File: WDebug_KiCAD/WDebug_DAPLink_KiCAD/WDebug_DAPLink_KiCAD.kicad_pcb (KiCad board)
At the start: 2 copper layers, 55 x 34 mm, 42 parts, among them J1 Conn_01x04, J2 Conn_02x04_UART_SW, J3 Conn_01x20_Female, J4 Conn_01x05_Male, J5 01x18_Female_Fan, P1 USB_C_Plug_USB2.0, SW1 SW_Rst, U1 AZ1117-3.3, U2 STM32F103C8Tx, Y1 8MHz

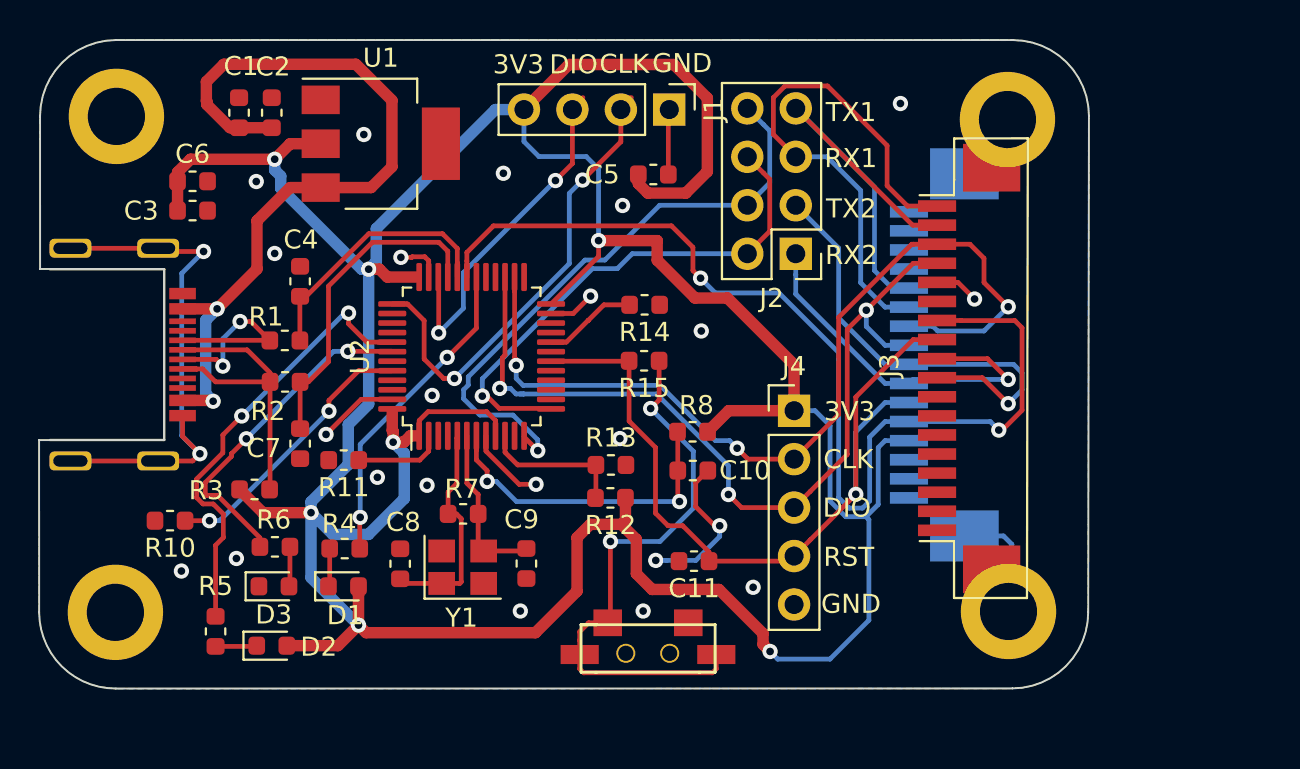
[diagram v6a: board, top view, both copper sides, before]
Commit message: WDebug_KiCAD_V1.3 修改串口RX和TX相反，16pin接口定义相反
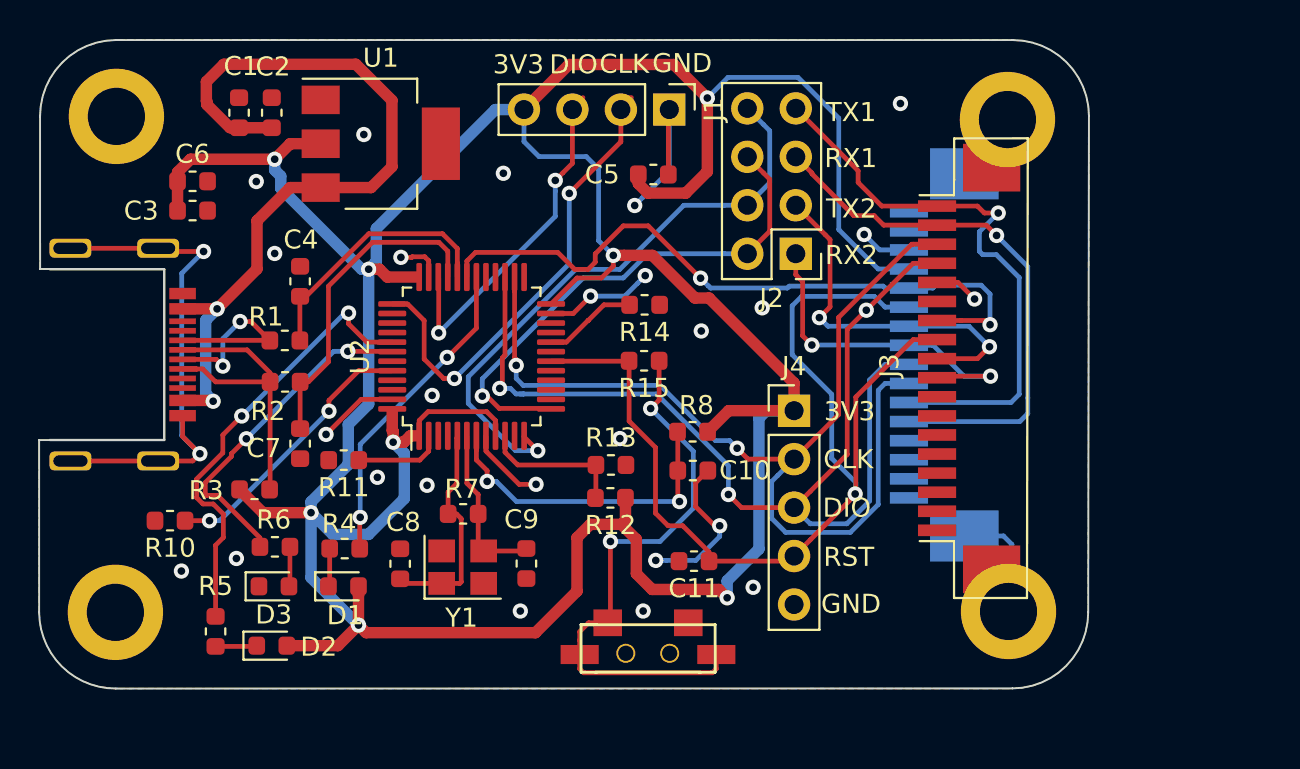
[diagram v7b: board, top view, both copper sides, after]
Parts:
- J5: footprint WDebug_KiCAD:1x16_P1.0mm -> WDebug_DAPLink:1x16_P1.0mm
- P1: footprint WDebug_KiCAD:USB-Type-C -> WDebug_DAPLink:USB-Type-C
- SW1: footprint WDebug_KiCAD:SWITCH_PUSH -> WDebug_DAPLink:SWITCH_PUSH
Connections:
- J3 pad 10: /RX2 -> /TX2
- J3 pad 17: /TX1 -> /RX1
- J3 pad 18: /RX1 -> /TX1
- J3 pad 9: /TX2 -> /RX2
- J5 pad 10: /RX2 -> /TX2
- J5 pad 5: /TX1 -> /RX1
- J5 pad 6: /RX1 -> /TX1
- J5 pad 9: /TX2 -> /RX2
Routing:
- net /T_SWO: track 55.7 -> 36.2 mm
- net /TG_RST: track 43.2 -> 55.3 mm
- net GND: track 36.9 -> 48.7 mm, vias 23 -> 26
- net /T_SWDIO: track 45.2 -> 55.3 mm
- net /TX1: track 22.3 -> 30.4 mm, vias 0 -> 1
- net /T_SWCLK: track 48.5 -> 54.7 mm, vias 3 -> 2
- net /TX2: track 23.9 -> 19.4 mm, vias 1 -> 2
- net /RX2: track 19.5 -> 18.0 mm, vias 1 -> 2
- net /T_TX: track 32.1 -> 31.5 mm
- net /RX1: track 28.3 -> 28.7 mm, vias 0 -> 1
- net +3V3: track 195.5 -> 195.8 mm, vias 7 -> 8
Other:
- board text added: "WDebug_DAPLink_V1.3 Chenweipeng 20200417"
- board text removed: "WDebug_DAPLink_V1.2 Chenweipeng 20200413"

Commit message: WDebug_DAPLink V1.4 1 修改 16Pin接口SWCLK和SWDIO反了。 2 3.3V不直接连接到16pin和18pin接口 3 AMS1117换成线性3819
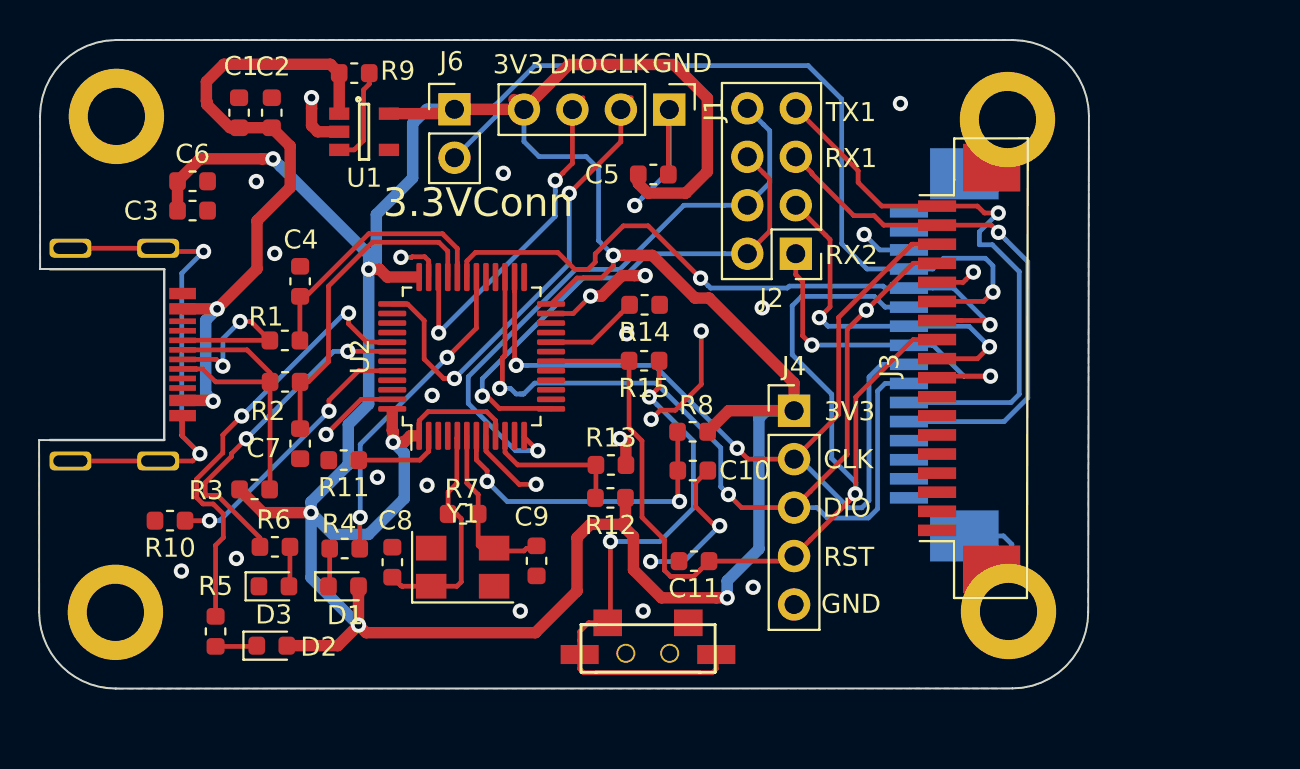
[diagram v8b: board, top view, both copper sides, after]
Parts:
- added J6: 3.3V_Conn, Connector_PinHeader_2.54mm:PinHeader_1x02_P2.54mm_Vertical, F.Cu at (115.8, 83.6)
- added R9: 10K, Resistor_SMD:R_0603_1608Metric, F.Cu at (110.5, 81.7)
- U1: value AZ1117-3.3 -> XC6228D332VR-G-matrix_display-rescue; footprint Package_TO_SOT_SMD:SOT-223 -> matrix_control_main:SOT23-5
- Y1: footprint Crystal:Crystal_SMD_3225-4Pin_3.2x2.5mm -> Crystal:Crystal_SMD_5032-4Pin_5.0x3.2mm
- moved U1 1.08 mm to (111.0, 84.8)
- moved C9 0.55 mm to (120.1, 107.3)
- moved C8 0.42 mm to (112.5, 107.4)
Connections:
- J3 pad 13: +3V3 -> /3_3V_Conn
- J5 pad 13: +3V3 -> /3_3V_Conn
- J5 pad 7: /T_SWCLK -> /T_SWDIO
- J5 pad 8: /T_SWDIO -> /T_SWCLK
- U1 pad 1: GND -> VBUS
- U1 pad 2: +3V3 -> GND
- U1 pad 3: VBUS -> Net-(R9-Pad1)
- U1 pad 4: (no net) -> Net-(U1-Pad4)
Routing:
- net /3_3V_Conn: track 0.00 -> 44.4 mm, vias 0 -> 1
- net +3V3: track 195.8 -> 180.3 mm, vias 8 -> 7
- net GND: track 48.7 -> 59.3 mm, vias 26 -> 28
- net VBUS: track 41.9 -> 34.9 mm
- net Net-(R9-Pad1): track 0.00 -> 5.13 mm
- net /T_SWCLK: track 54.7 -> 50.4 mm
- net /TG_RST: track 55.3 -> 57.1 mm
- net /T_SWO: track 36.2 -> 35.1 mm
- net Net-(C9-Pad1): track 8.69 -> 9.29 mm
- net Net-(C8-Pad1): track 11.7 -> 12.3 mm
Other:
- board text added: "3.3VConn"
- board text added: "WDebug_DAPLink_V1.4 Chenweipeng 20200515"
- board text removed: "TX2"
- board text removed: "WDebug_DAPLink_V1.3 Chenweipeng 20200417"
